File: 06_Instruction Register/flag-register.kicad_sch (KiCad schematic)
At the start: 11 parts, among them U4 74LS157, U5 74LS173, U6 74LS245

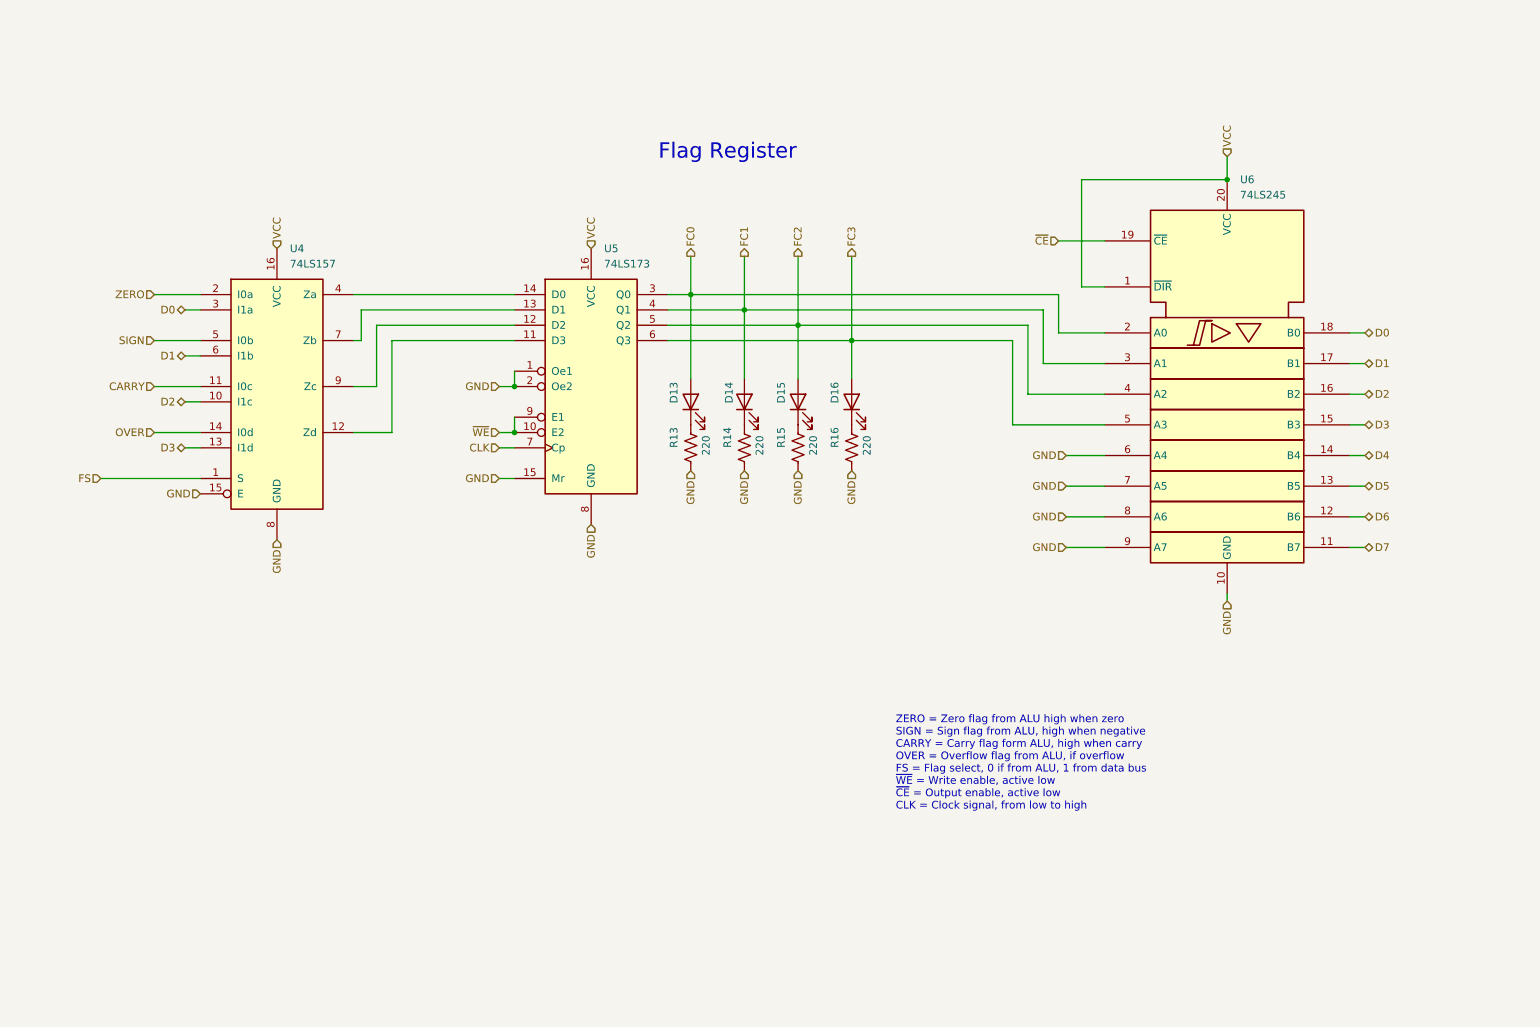
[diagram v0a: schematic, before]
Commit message: Last revision of the cpu, all boards have been ordered. Implementation to be tested and documented in following commits.
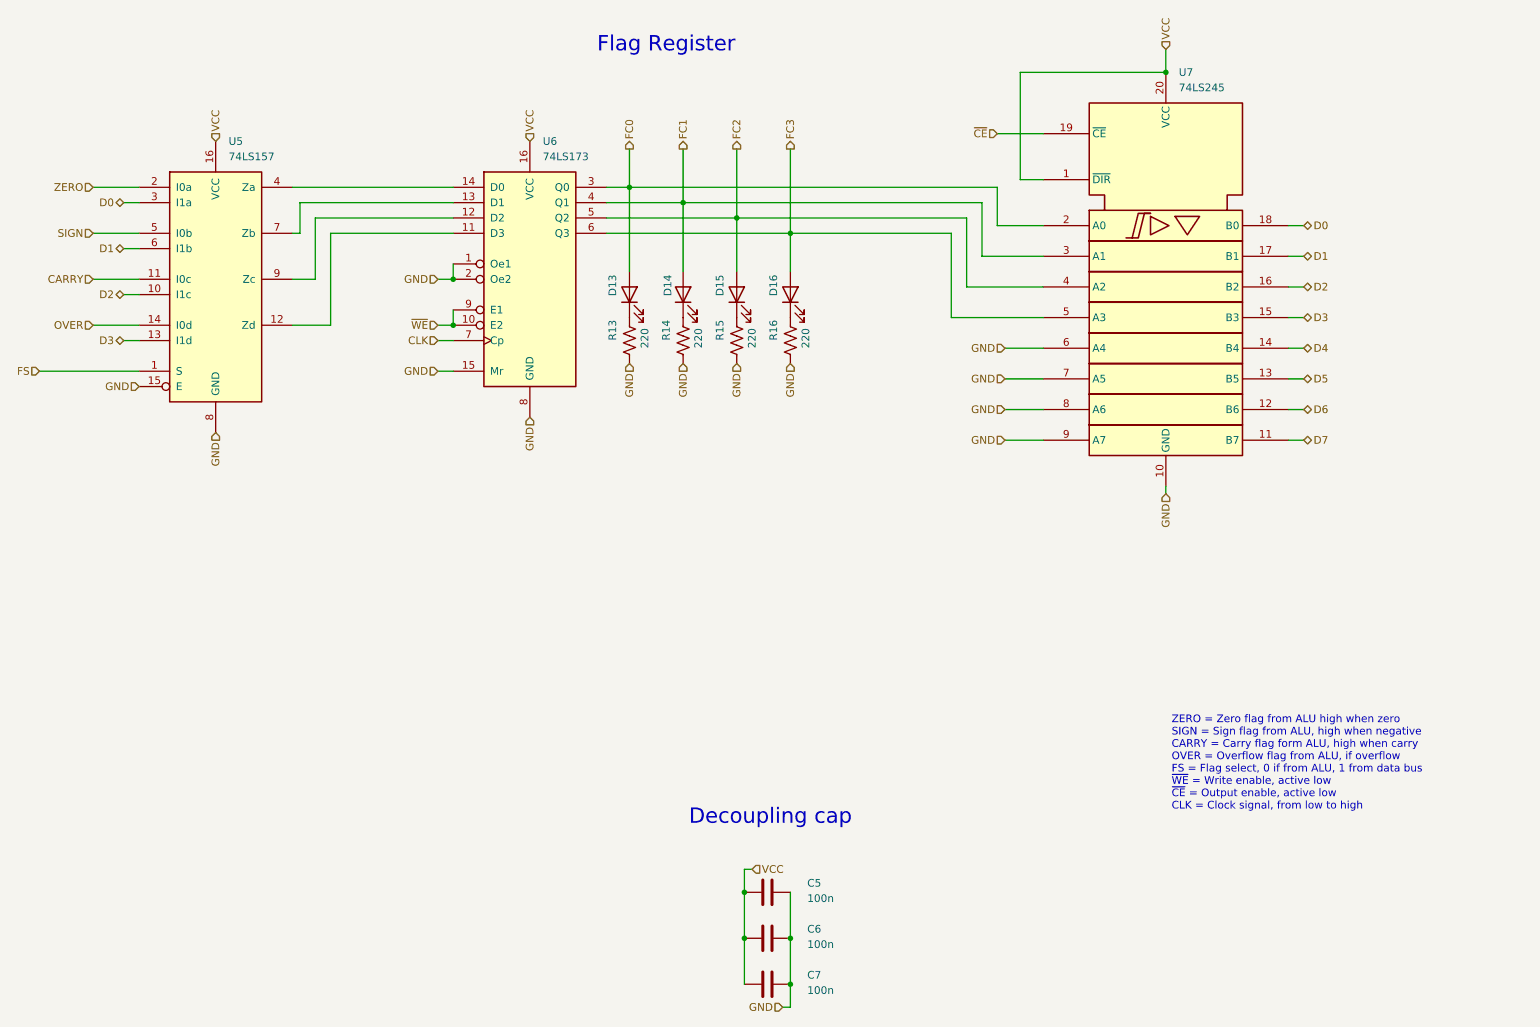
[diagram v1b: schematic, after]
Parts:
- added C5, C6, C7: 100n, Capacitor_THT:C_Disc_D3.0mm_W1.6mm_P2.50mm, symbol Device:C
- renumbered U4 to U5, U5 to U6, U6 to U7
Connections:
- net GND: now also C5.2, C6.2, C7.2
- net VCC: now also C5.1, C6.1, C7.1
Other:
- note added: "Decoupling cap"
- moved on the sheet: D13, D14, D15, D16, R13, R14, R15, R16, U5, U6, U7
